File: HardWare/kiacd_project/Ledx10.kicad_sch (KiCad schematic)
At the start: 49 parts, among them J1 POWER_IN, U1 TPS923651

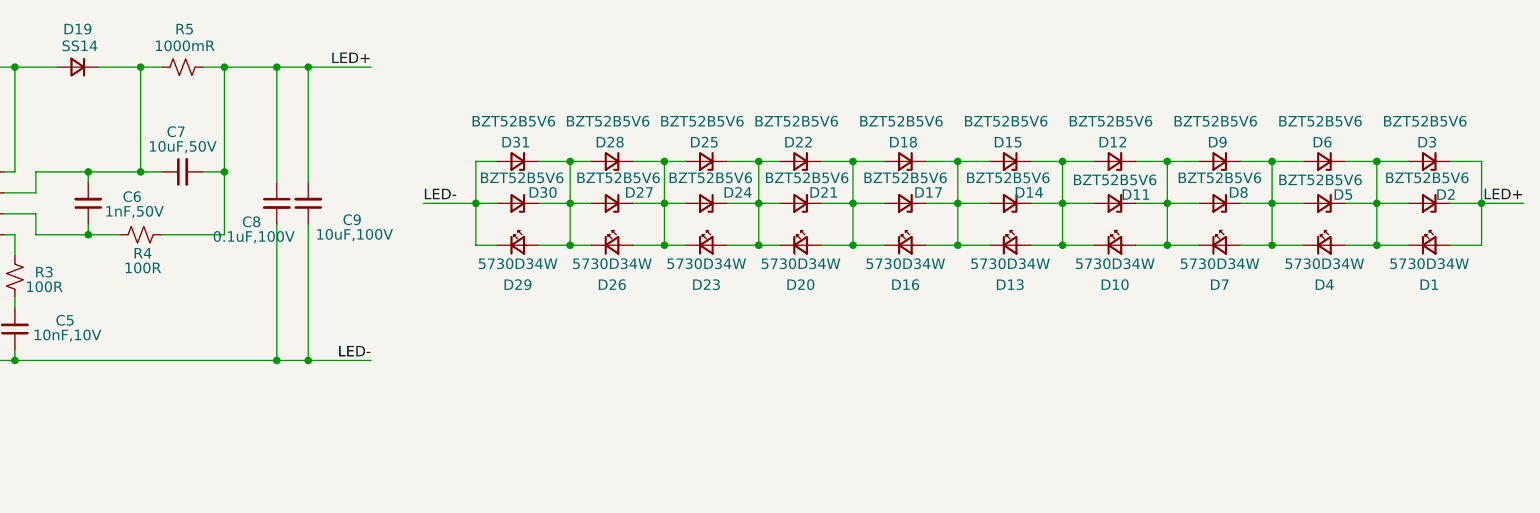
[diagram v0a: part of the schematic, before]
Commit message: 更新电路设计LED增加到20pix
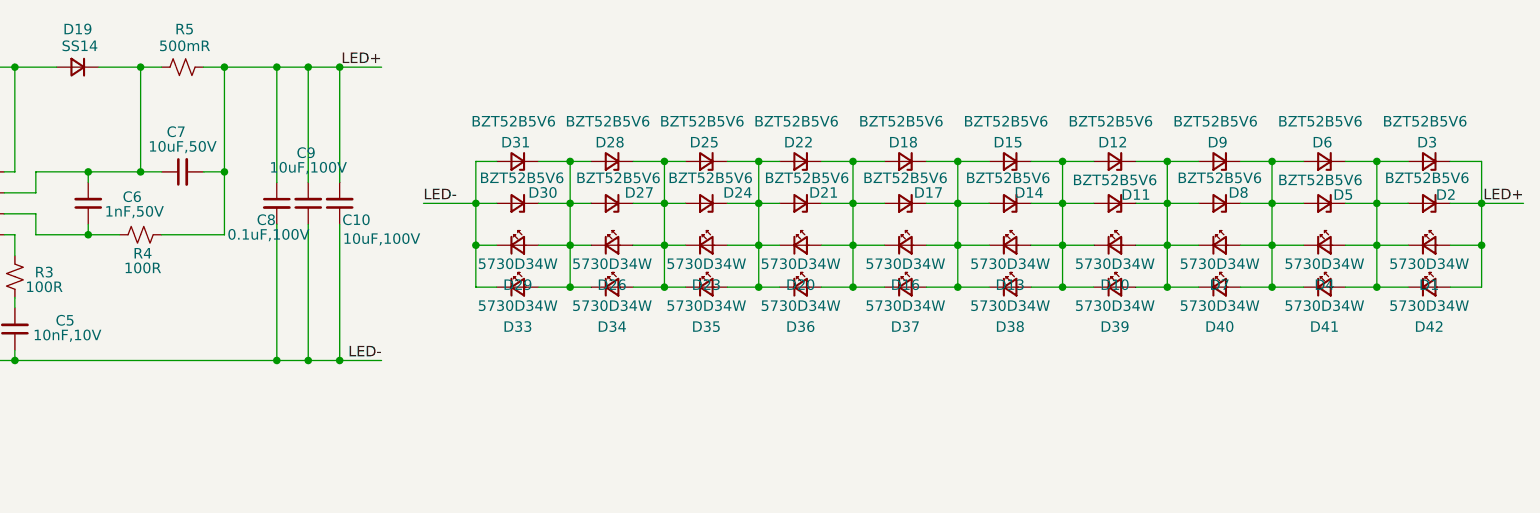
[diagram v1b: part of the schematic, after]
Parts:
- added C10: 10uF,100V, Capacitor_SMD:C_0805_2012Metric, symbol Device:C_Small
- added D33, D34, D35, D36, D37, D38, D39, D40, D41, D42: 5730D34W, 3rd_LED_SMD:LED5730_2012Metric, symbol Device:LED_Small
- L1: footprint Inductor_SMD:L_1206_3216Metric -> Inductor_SMD:L_Taiyo-Yuden_MD-3030
- R5: value 1000mR -> 500mR
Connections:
- net GND: now also C10.1, D33.1 (K)
- net LED+: now also C10.2, D42.2 (A)
- net at D4.1 (K), D5.2 (A), D6.2 (A)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: now also D40.2 (A), D41.1 (K)
- net at D10.2 (A), D11.1 (K), D12.1 (K)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: now also D39.2 (A), D40.1 (K)
- net at D1.1 (K), D2.2 (A), D3.2 (A)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: now also D41.2 (A), D42.1 (K)
- net at D10.1 (K), D11.2 (A), D12.2 (A)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: now also D38.2 (A), D39.1 (K)
- net at D13.1 (K), D14.2 (A), D15.2 (A)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: now also D37.2 (A), D38.1 (K)
- net at D16.1 (K), D17.2 (A), D18.2 (A)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: now also D36.2 (A), D37.1 (K)
- net at D20.1 (K), D21.2 (A), D22.2 (A)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: now also D35.2 (A), D36.1 (K)
- net at D26.1 (K), D27.2 (A), D28.2 (A)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: now also D33.2 (A), D34.1 (K)
- net at D23.1 (K), D24.2 (A), D25.2 (A)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: now also D34.2 (A), D35.1 (K)

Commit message: 更新PCB设计，增加LED并联，增强光照强度
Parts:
- R5: footprint Resistor_SMD:R_0805_2012Metric -> Resistor_SMD:R_1206_3216Metric
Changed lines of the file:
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@@
 			)
 		)
-		(property "Footprint" "Resistor_SMD:R_0805_2012Metric"
+		(property "Footprint" "Resistor_SMD:R_1206_3216Metric"
 			(at 118.11 74.93 0)
 			(effects

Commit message: 更新LED5730封装错误，手册没有说明散热焊盘与阳极相连
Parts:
- C10, C9: footprint Capacitor_SMD:C_0805_2012Metric -> Capacitor_SMD:C_1206_3216Metric
- L1: value SCL3216T330KSP,33uH -> SMMS0650-680M,68uH; footprint Inductor_SMD:L_Taiyo-Yuden_MD-3030 -> Inductor_SMD:L_6.3x6.3_H3
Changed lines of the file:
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@@
 			)
 		)
-		(property "Value" "SCL3216T330KSP,33uH"
+		(property "Value" "SMMS0650-680M,68uH"
 			(at 81.28 72.39 90)
 			(effects
@@
 			)
 		)
-		(property "Footprint" "Inductor_SMD:L_Taiyo-Yuden_MD-3030"
+		(property "Footprint" "Inductor_SMD:L_6.3x6.3_H3"
 			(at 81.28 74.93 0)
 			(effects
@@
 			)
 		)
-		(property "Footprint" "Capacitor_SMD:C_0805_2012Metric"
+		(property "Footprint" "Capacitor_SMD:C_1206_3216Metric"
 			(at 133.35 91.44 0)
 			(effects
@@
 			)
 		)
-		(property "Footprint" "Capacitor_SMD:C_0805_2012Metric"
+		(property "Footprint" "Capacitor_SMD:C_1206_3216Metric"
 			(at 137.16 91.44 0)
 			(effects
